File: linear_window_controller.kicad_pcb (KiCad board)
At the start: 4 copper layers, 114.3 x 86.4 mm, 168 parts, among them J1 Motor 2, J10 DCDC_IN, J11 VBus, J12 VCC, J13 GND, J14 PANEL_BTN, J2 Motor 1, J3 Motor 4, J4 Motor 3, J5 Amphenol 10053363-200LF, J6 ATX-24 (Molex 39-28-1243), J7 Link-PP_LPJ0135GDNL, J8 PANEL_LED, J9 Control, P1 ESP32 USB, P2 CONSOLE, Q1 BC817-40(SOT23), Q2 BC817-40(SOT23), Q3 BSS138, Q4 BSS138, SW1 PGM, SW2 Service, SW3 Service, SW4 Service, SW5 Service, SW7 Service, U1 TSOP384xx, U10 TMP100, U11 CP2102N-A01-GQFN24, U12 93LC46BT-E/OT, U13 DM9051, U2 DRV8874, U3 DRV8874, U4 DRV8874, U5 DRV8874, U6 PCF8574APWRG4, U7 LIS3DH, U8 ESP32-S3-WROOM-1-N16R2, U9 TPS562200, Y1 25MHz YXC X322525MOB4SI

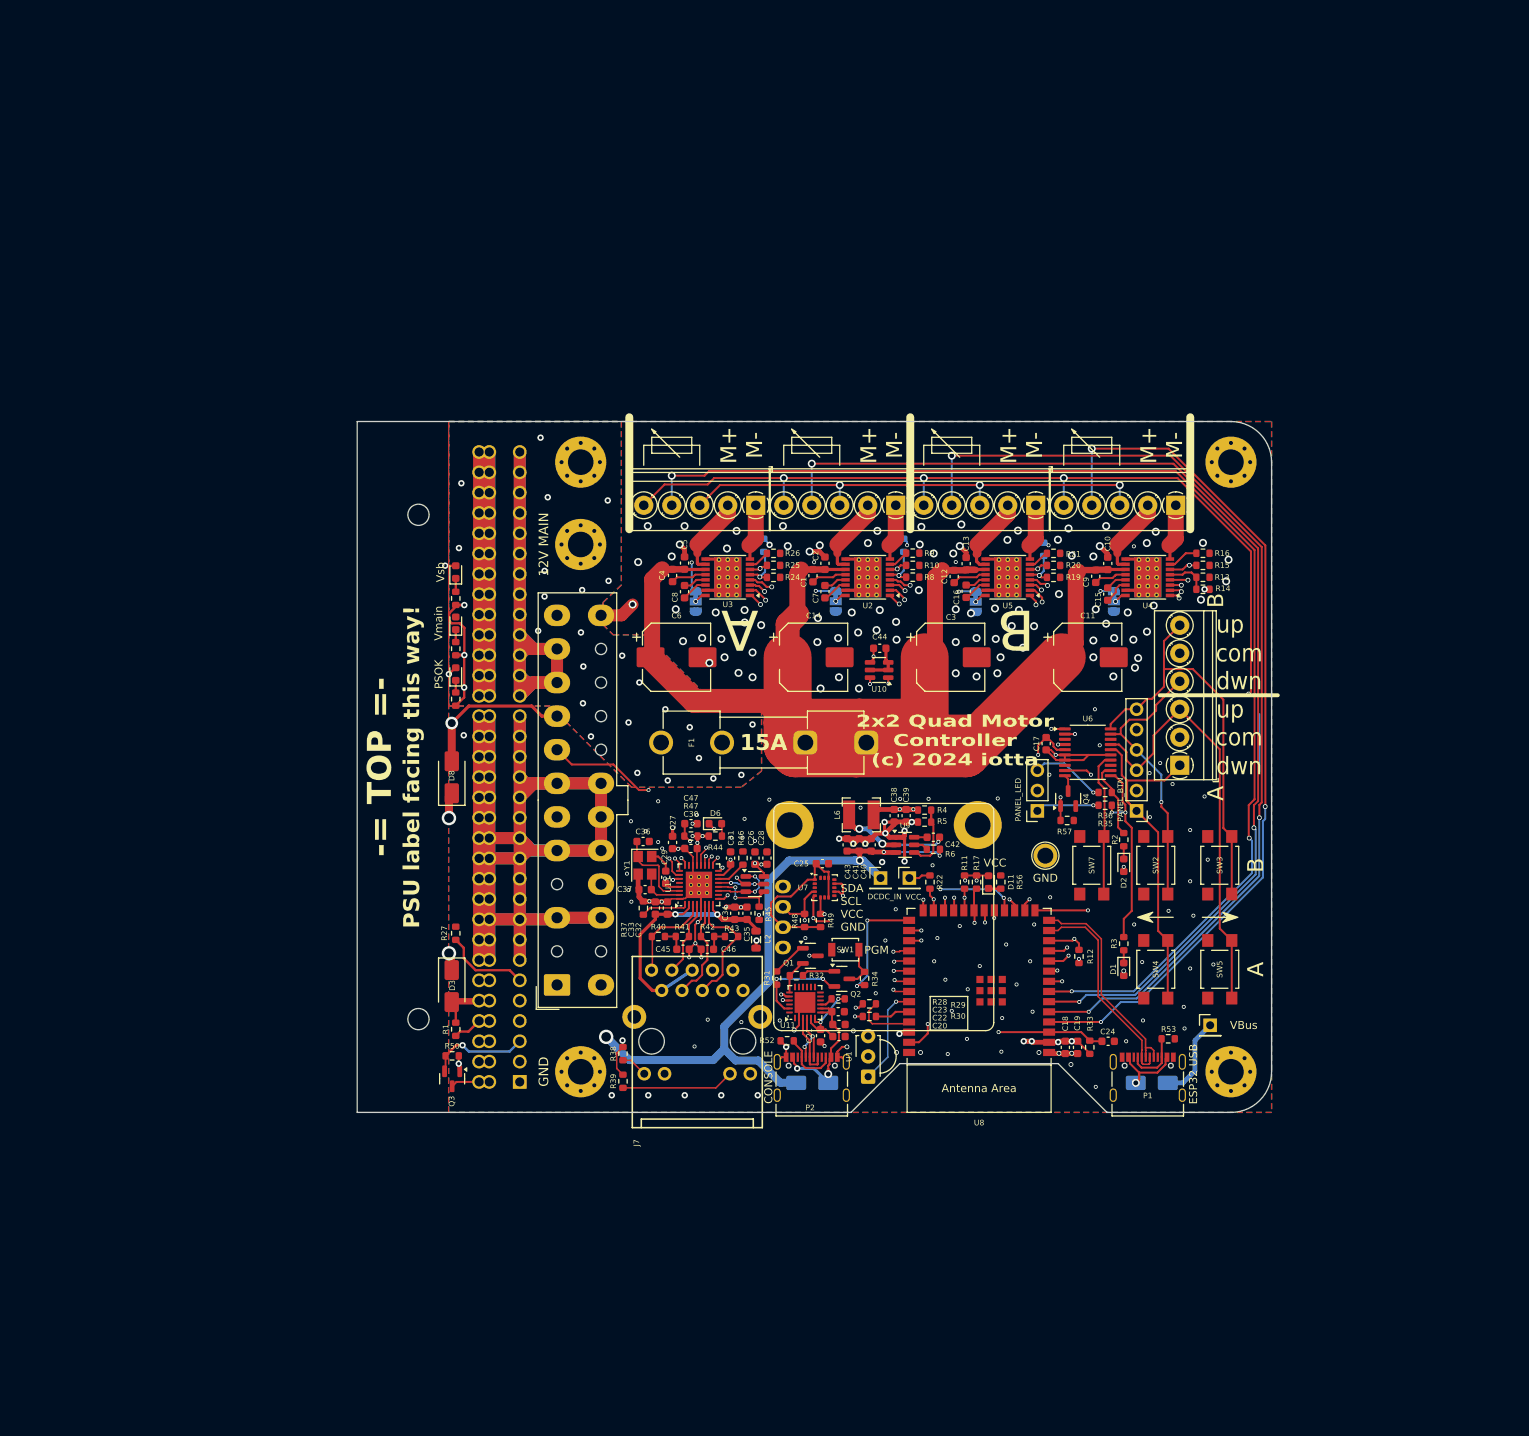
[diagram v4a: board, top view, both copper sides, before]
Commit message: Add channel indication LEDs Add external IO (2 inputs/low power IO, 2 high power OD outputs for e.g. magnetic locks) Swap PCF8574 for PCA9555 16 bit iot expander Add heatsink to board (3D) Add PDF file of V1 schematics
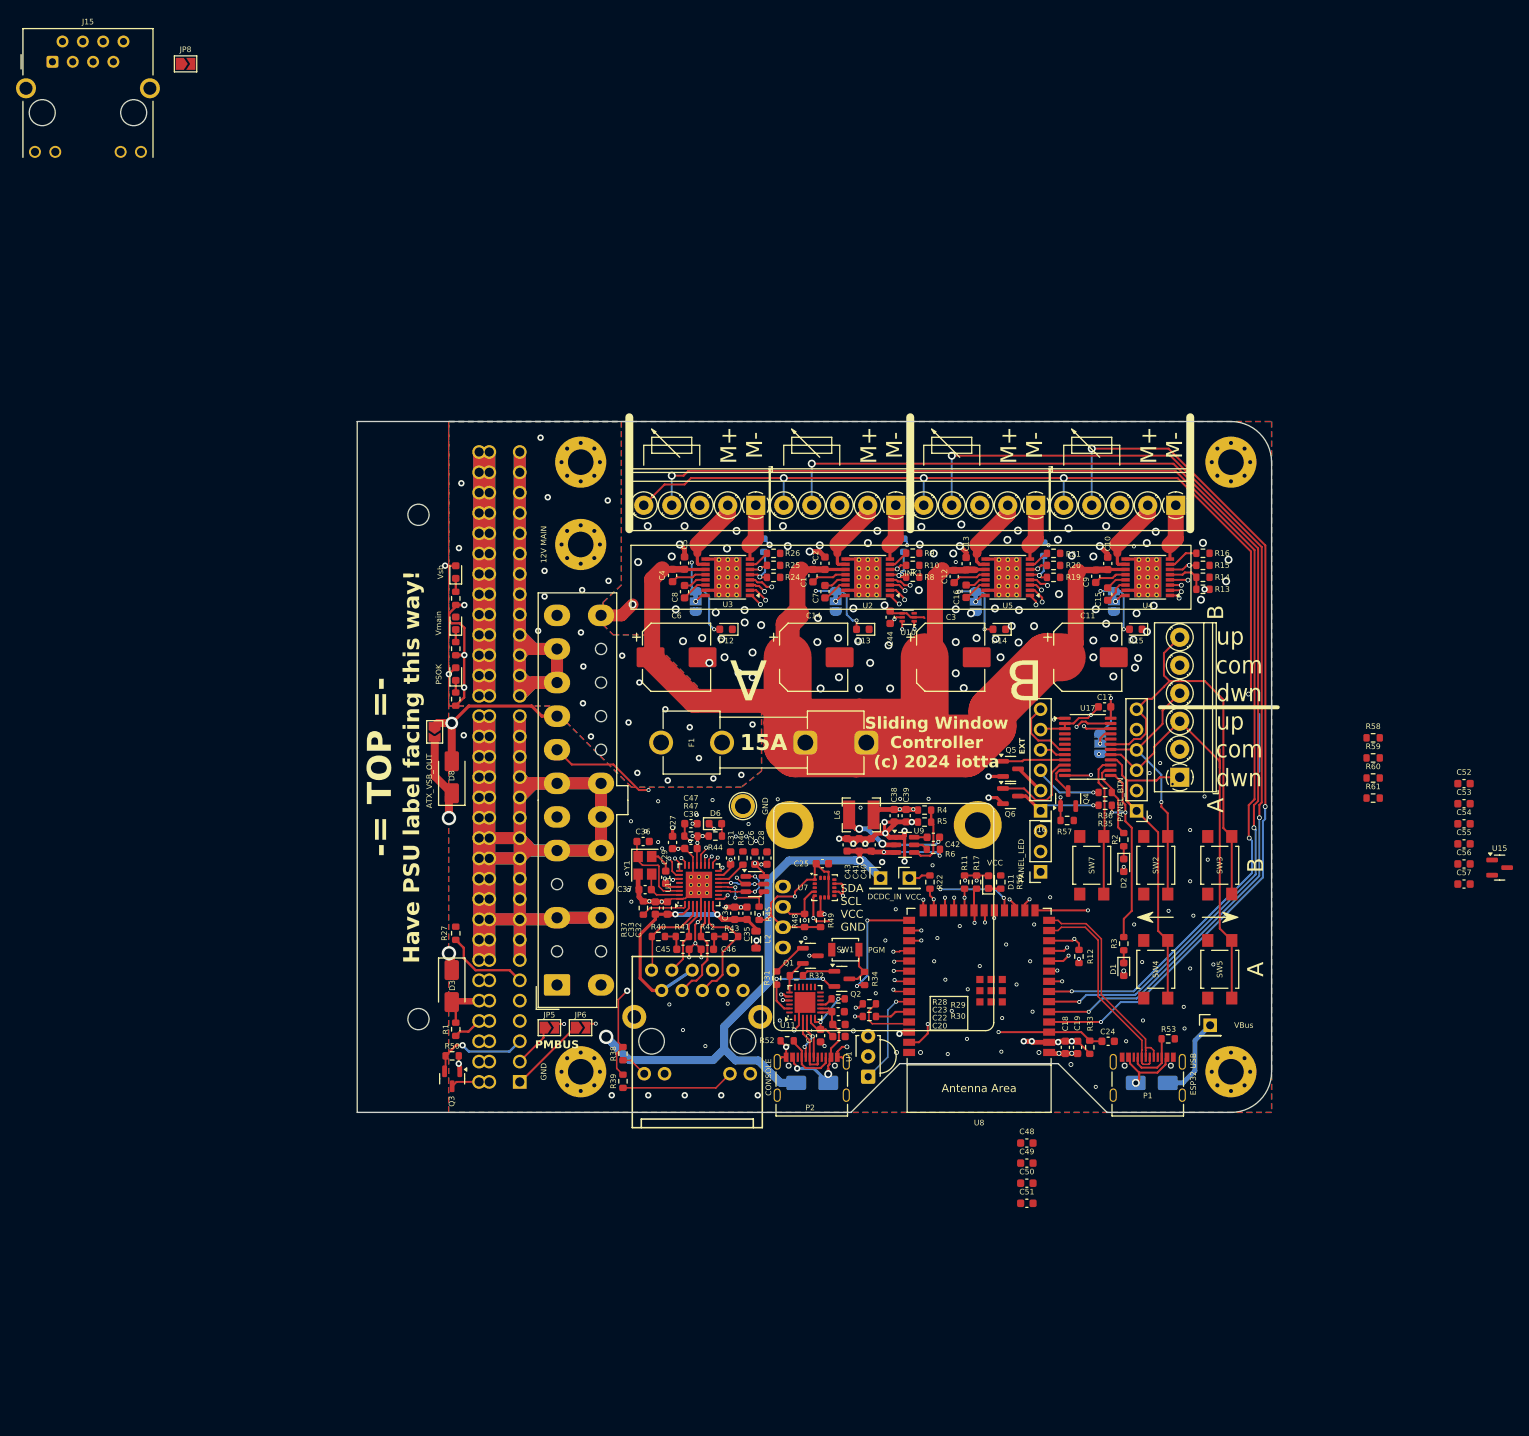
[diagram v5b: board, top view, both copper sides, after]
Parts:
- removed U6: PCF8574APWRG4, Package_SO:TSSOP-20_4.4x6.5mm_P0.65mm
- added C48: 10n, Capacitor_SMD:C_0603_1608Metric, F.Cu at (126.9, 139.7)
- added C49: 10n, Capacitor_SMD:C_0603_1608Metric, F.Cu at (126.9, 142.2)
- added C50: 10n, Capacitor_SMD:C_0603_1608Metric, F.Cu at (126.9, 144.7)
- added C51: 10n, Capacitor_SMD:C_0603_1608Metric, F.Cu at (126.9, 147.2)
- added C52: 1u, Capacitor_SMD:C_0603_1608Metric, F.Cu at (181.5, 94.8)
- added C53: 1u, Capacitor_SMD:C_0603_1608Metric, F.Cu at (181.5, 97.3)
- added C54: 1u, Capacitor_SMD:C_0603_1608Metric, F.Cu at (181.5, 99.8)
- added C55: 1u, Capacitor_SMD:C_0603_1608Metric, F.Cu at (181.5, 102.3)
- added C56: 1u, Capacitor_SMD:C_0603_1608Metric, F.Cu at (181.5, 104.8)
- added C57: 1u, Capacitor_SMD:C_0603_1608Metric, F.Cu at (181.5, 107.3)
- added D12: A1, LED_SMD:LED_0603_1608Metric, F.Cu at (89.3, 75.5)
- added D13: A2, LED_SMD:LED_0603_1608Metric, F.Cu at (106.4, 75.5)
- added D14: B1, LED_SMD:LED_0603_1608Metric, F.Cu at (123.4, 75.5)
- added D15: B2, LED_SMD:LED_0603_1608Metric, F.Cu at (140.5, 75.5)
- added J15: RJ45_Hanrun_HR911105A_Horizontal, Connector_RJ:RJ45_Hanrun_HR911105A_Horizontal, F.Cu at (5.08, 4.57)
- added J16: EXT, Connector_PinHeader_2.54mm:PinHeader_1x06_P2.54mm_Vertical, F.Cu at (128.6, 98.2)
- added JP5: PMBUS_DA, Jumper:SolderJumper-2_P1.3mm_Open_TrianglePad1.0x1.5mm, F.Cu at (67.2, 125.3)
- added JP6: PMBUS_CL, Jumper:SolderJumper-2_P1.3mm_Open_TrianglePad1.0x1.5mm, F.Cu at (71.1, 125.3)
- added JP7: ATX_VSB_OUT, Jumper:SolderJumper-2_P1.3mm_Open_TrianglePad1.0x1.5mm, F.Cu at (52.9, 88.3)
- added JP8: PSMB_ADDR, Jumper:SolderJumper-2_P1.3mm_Open_TrianglePad1.0x1.5mm, F.Cu at (21.7, 4.83)
- added JP9: ADDR, Jumper:SolderJumper-3_P1.3mm_Bridged12_RoundedPad1.0x1.5mm, B.Cu at (136.1, 89.8)
- added Q5: Si2318CDS, Package_TO_SOT_SMD:SOT-23, F.Cu at (124.8, 93.0)
- added Q6: Si2318CDS, Package_TO_SOT_SMD:SOT-23, F.Cu at (124.8, 96.3)
- added R58: 300, Resistor_SMD:R_0603_1608Metric, F.Cu at (170.2, 89.1)
- added R59: 300, Resistor_SMD:R_0603_1608Metric, F.Cu at (170.2, 91.6)
- added R60: 300, Resistor_SMD:R_0603_1608Metric, F.Cu at (170.2, 94.1)
- added R61: 300, Resistor_SMD:R_0603_1608Metric, F.Cu at (170.2, 96.6)
- added SINK1: heatsink_window_controller_70x8mm, iotta_footprints_v6:heatsink_window_controller_70x8mm, F.Cu at (112.4, 69.0)
- added U15: MCP1703Ax-250xxTT, Package_TO_SOT_SMD:SOT-23, F.Cu at (186.0, 105.3)
- added U17: PCA9555PW, Package_SO:TSSOP-24_4.4x7.8mm_P0.65mm, F.Cu at (134.5, 90.2)
- L6: value 2.2µ -> 4.7µ
- R10, R15, R20, R25: value TBD -> 1.1k
- R11, R12, R17, R22: value TBD -> 10k
- R13, R18, R23, R7: value TBD -> 16k
- R14, R19, R24, R8: value TBD -> 49.9k
- R2, R3, R35, R36, R56: value 100 -> 300
- R51, R54: value 300 -> 470
- U10: value TMP100 -> TMP112AIDRLR; footprint Package_TO_SOT_SMD:SOT-23-6 -> Package_TO_SOT_SMD:SOT-563
- moved J13 38.3 mm to (91.4, 97.6), turned to 90 degrees
- moved C17 8.63 mm to (136.6, 85.2), turned to 180 degrees
- moved J8 7.63 mm to (128.6, 105.8)
- moved U10 7.52 mm to (112.0, 74.0)
- moved C44 4.09 mm to (109.8, 74.0), turned to 90 degrees
- moved J9 1.50 mm to (146.0, 94.0)
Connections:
- J1 pad 5: +3.3V -> +POT_2.5V
- J2 pad 5: +3.3V -> +POT_2.5V
- J3 pad 5: +3.3V -> +POT_2.5V
- J4 pad 5: +3.3V -> +POT_2.5V
- U10 pad 3: GND -> unconnected-(U10-ALERT-Pad3)
- U10 pad 4: +3.3V -> GND
- U10 pad 5: GND -> +3.3V
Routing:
- net +POT_2.5V: track 0.00 -> 109.3 mm, vias 0 -> 4
- net +3.3V: track 340.4 -> 255.8 mm, vias 40 -> 41
- net GND: track 547.2 -> 483.1 mm, vias 202 -> 198
- net /SDA: track 102.4 -> 155.1 mm, vias 4 -> 5
- net /SCL: track 104.2 -> 151.2 mm, vias 4 -> 5
- net /EXT_OUT2: track 0.00 -> 11.8 mm
- net /PS_SCL: track 0.00 -> 9.68 mm
- net /EXT_IN1: track 0.00 -> 8.55 mm
- net /EXT_OUT1: track 0.00 -> 7.80 mm
- net /DCDC_IN: track 181.7 -> 189.0 mm
- net /PS_SDA: track 0.00 -> 5.47 mm
- net /EXT_OUT1_OD: track 0.00 -> 3.94 mm
- net /EXT_OUT2_OD: track 0.00 -> 3.59 mm
- net /EXT_IN2: track 0.00 -> 3.28 mm
- net /B_UP: track 34.6 -> 32.2 mm
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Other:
- board text added: "Have PSU label facing this way!"
- board text added: "PMBUS"
- board text added: "Sliding Window Controller (c) 2024 iotta"
- board text removed: "2x2 Quad Motor Controller (c) 2024 iotta"
- board text removed: "PSU label facing this way!"

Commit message: Update PCB to reflect the v2.x update Included PMbus voltage shifter (5V <-> 3.3V)
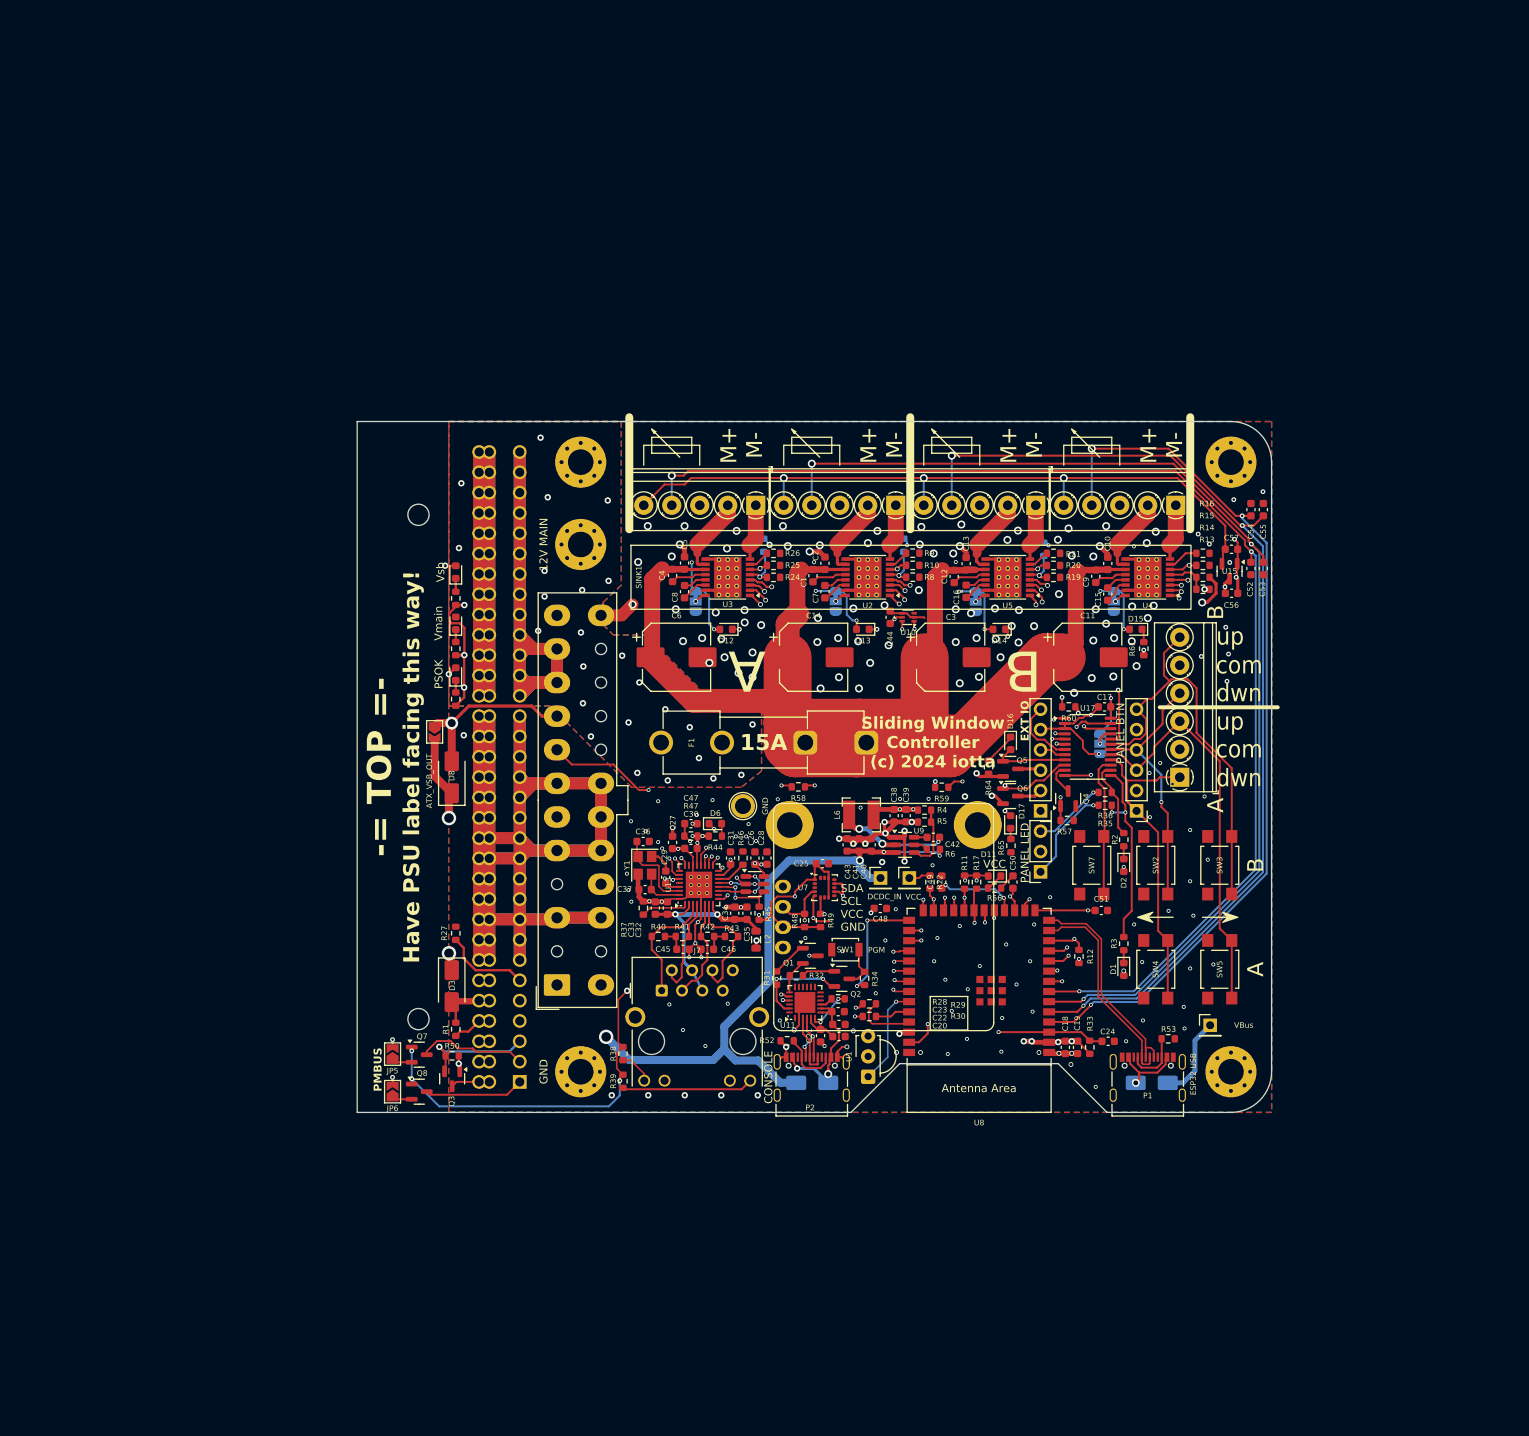
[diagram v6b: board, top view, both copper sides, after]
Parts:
- removed J15: RJ45_Hanrun_HR911105A_Horizontal, Connector_RJ:RJ45_Hanrun_HR911105A_Horizontal
- removed JP8: PSMB_ADDR, Jumper:SolderJumper-2_P1.3mm_Open_TrianglePad1.0x1.5mm
- added D16: EXT1, LED_SMD:LED_0603_1608Metric, F.Cu at (124.8, 89.8)
- added D17: EXT2, LED_SMD:LED_0603_1608Metric, F.Cu at (124.8, 99.6)
- added Q7: BSS138, Package_TO_SOT_SMD:SOT-23, F.Cu at (50.9, 128.7)
- added Q8: BSS138, Package_TO_SOT_SMD:SOT-23, F.Cu at (50.9, 133.3)
- added R64: 300, Resistor_SMD:R_0603_1608Metric, F.Cu at (122.1, 92.7)
- added R65: 300, Resistor_SMD:R_0603_1608Metric, F.Cu at (124.9, 102.5)
- J14: value PANEL_BTN -> PANEL BTN
- J16: value EXT -> EXT IO
- J7: value Link-PP_LPJ0135GDNL -> RJ45_Hanrun_HR911105A_Horizontal; footprint iotta_footprints:LinkPP_LPJ0135GDNL -> Connector_RJ:RJ45_Hanrun_HR911105A_Horizontal
- J8: value PANEL_LED -> PANEL LED
- moved R58 72.1 mm to (98.3, 95.2), turned to 180 degrees
- moved R59 54.0 mm to (116.2, 95.2), turned to 180 degrees
- moved C57 50.9 mm to (152.5, 65.5)
- moved U15 50.1 mm to (152.2, 68.3), turned to -90 degrees
- moved C55 48.7 mm to (156.4, 60.5), turned to 90 degrees
- moved C54 47.4 mm to (154.9, 60.5), turned to 90 degrees
- moved C56 44.6 mm to (152.5, 71.0)
- moved R60 39.1 mm to (132.1, 85.2), turned to 180 degrees
- moved C53 38.6 mm to (156.4, 67.9), turned to -90 degrees
- moved C52 37.8 mm to (154.9, 67.9), turned to -90 degrees
- moved C51 37.8 mm to (136.2, 110.7)
- moved C50 37.7 mm to (125.2, 107.1), turned to 90 degrees
- moved C49 36.7 mm to (116.2, 107.1), turned to 90 degrees
- moved C48 34.6 mm to (108.6, 110.4)
- moved R61 34.2 mm to (141.5, 77.9), turned to 90 degrees
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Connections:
- net /PS_ON renamed /~{PS_ON}
- J16 pad 1: /EXT_OUT2_OD -> GND
- J16 pad 2: /EXT_OUT1_OD -> /EXT_OUT2_OD
- J16 pad 3: GND -> /EXT_OUT1_OD
- J7 pad 10: unconnected-(J7-VC2--Pad10) -> /LAN_ACT
- J7 pad 11: Net-(J7-LED1_A) -> /LAN_SPEED
- J7 pad 12: /LAN_ACT -> Net-(J7-Pad12)
- J7 pad 2: AVDD -> Net-(J7-TD-)
- J7 pad 3: Net-(J15-RD-) -> Net-(J7-RD+)
- J7 pad 4: Net-(J15-TD+) -> AVDD
- J7 pad 8: unconnected-(J7-VC1--Pad8) -> GND
- J7 pad 9: unconnected-(J7-VC2+-Pad9) -> Net-(J7-Pad9)
- JP5 pad 1: /PS_SDA -> Net-(JP5-A)
- JP6 pad 1: /PS_SCL -> Net-(JP6-A)
- R38 pad 1: Net-(J7-LED1_A) -> Net-(J7-Pad9)
- R39 pad 1: Net-(J7-LED2_A) -> Net-(J7-Pad12)
- R41 pad 2: Net-(J15-RD-) -> Net-(J7-TD-)
- R42 pad 2: Net-(J15-TD+) -> Net-(J7-RD+)
- U13 pad 4: Net-(J15-RD-) -> Net-(J7-TD-)
- U13 pad 6: Net-(J15-TD+) -> Net-(J7-RD+)
- U17 pad 4: /LED_A1 -> /LED_A2
- U17 pad 5: /LED_A2 -> /LED_A1
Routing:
- net +3.3V: track 255.8 -> 296.6 mm, vias 41 -> 45
- net /LED_A1: track 0.00 -> 36.1 mm, vias 0 -> 2
- net /SCL: track 151.2 -> 180.4 mm
- net Net-(D13-K): track 0.00 -> 24.5 mm, vias 0 -> 2
- net Net-(D12-K): track 0.00 -> 24.2 mm, vias 0 -> 2
- net /SDA: track 155.1 -> 178.5 mm
- net +POT_2.5V: track 109.3 -> 91.7 mm, vias 4 -> 3
- net /LED_A2: track 0.00 -> 17.5 mm, vias 0 -> 2
- net Net-(J7-Pad12): track 0.00 -> 16.4 mm
- net GND: track 483.1 -> 498.7 mm, vias 198 -> 207
- net /LED_B2: track 0.00 -> 14.3 mm, vias 0 -> 2
- net Net-(D14-K): track 0.00 -> 14.3 mm, vias 0 -> 2
- net Net-(J7-LED2_A): track 14.1 -> 0.00 mm
- net Net-(J7-RD+): track 0.00 -> 12.9 mm
- net Net-(J15-TD+): track 12.9 -> 0.00 mm
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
